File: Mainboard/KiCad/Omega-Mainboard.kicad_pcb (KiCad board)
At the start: 2 copper layers, 333.4 x 149.9 mm, 248 parts, among them J1 5V, J10 POWER, J11 KEYBOARD, J12 RAM_EXT, J13 ~RST~/~NMI, J14 CBUS, J2 Composite, J3 Audio, J4 S-VIDEO, J5 RGB, J6 Cassette, J7 JOYSTICK_A, J8 JOYSTICK_B, J9 PRINTER, Q1 PN2907A, Q2 PN2907A, U1 Z84C00, U10 D41464, U11 D41464, U12 ATF16V8B, U13 ATF16V8B, U14 ATF16V8B, U15 74HCT670, U16 74HCT670, U17 74HCT670, U18 74HCT670, U19 74F541, U2 82C55, U20 74F541, U21 74F541, U22 74HCT540, U23 74HCT273, U24 74HCT273, U25 74F245, U26 74F245, U27 74HCT175, U28 74HCT157, U29 74HCT157, U3 V9938/V9958, U30 74HCT153, U31 74HCT153, U32 74AHCT138, U33 74AHCT125, U34 74HCT74, U35 74HCT74, U36 74HCT74, U37 74AHCT32, U38 74AHCT32, U39 74AHCT32, U4 YM2149, U40 74HCT30, U41 74HCT30, U42 74LS07, U43 74HCT04, U44 74AHCT02, U45 74HCT00, U46 ADM691A, U47 CXA1645, U48 MCP6281, U49 LM311, U5 RP5C01, U6 SST39SF040, U7 AS6C4008, U8 D41464, U9 D41464, Y1 21.477270MHz, Y2 32768 Hz, Y3 4.433618MHz

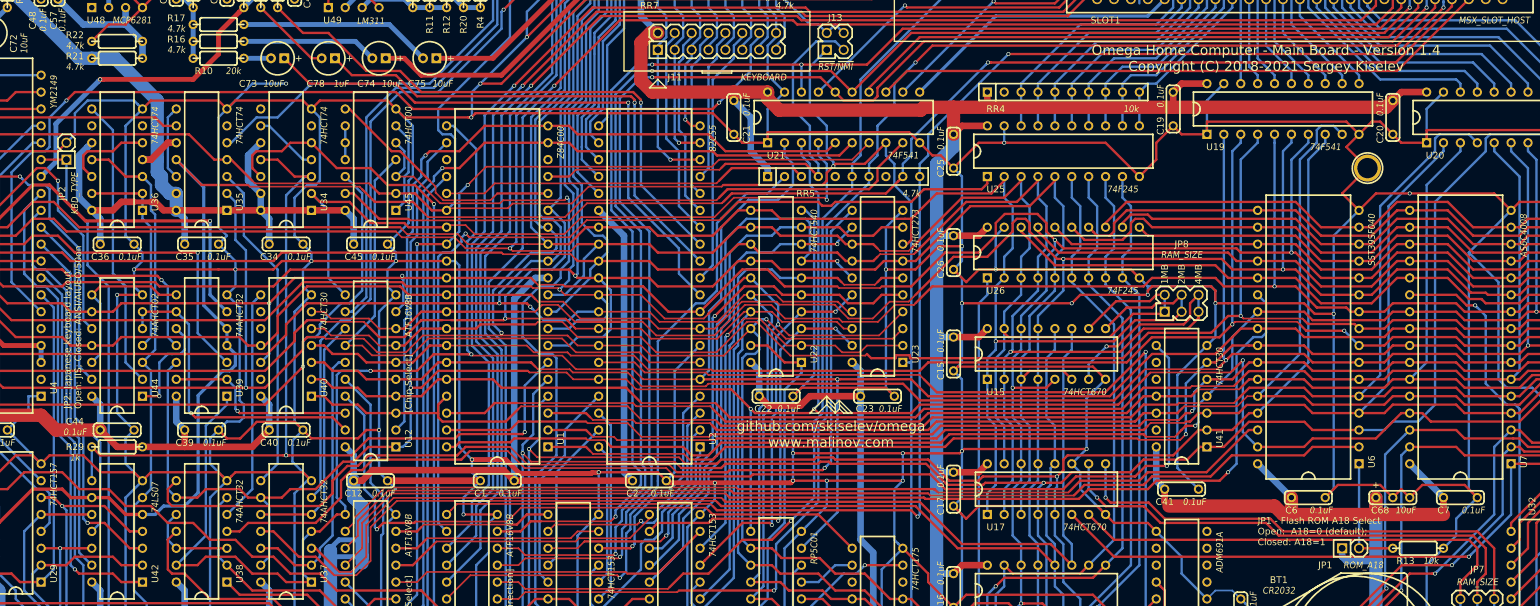
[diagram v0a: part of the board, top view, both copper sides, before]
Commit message: Fix issue #56, where joystick A trigger 2 was swapped with joystick B trigger 1
Signed-off-by: Sergey Kiselev <skiselev@gmail.com>
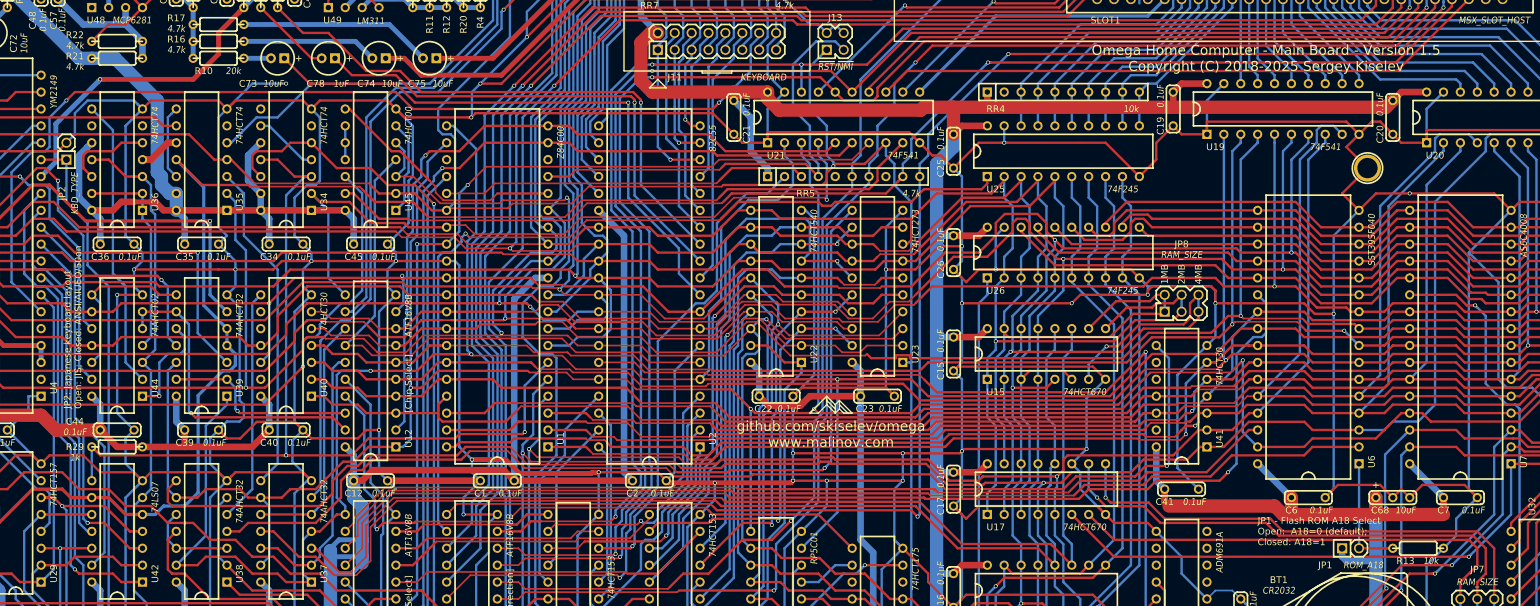
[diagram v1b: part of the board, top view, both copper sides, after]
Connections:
- U42 pad 11: /PSG/JB2 -> /PSG/JB1
- U42 pad 13: /PSG/JB1 -> /PSG/JB2
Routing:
- net /PSG/JB2: track 49.9 -> 55.5 mm
- net /PSG/JB1: track 58.3 -> 53.6 mm
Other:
- board text added: "Omega Home Computer - Main Board - Version 1.5 Copyright (C) 2018-2025 Sergey Kiselev"
- board text removed: "Omega Home Computer - Main Board - Version 1.4 Copyright (C) 2018-2021 Sergey Kiselev"

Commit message: Update gerber files for version 1.5
Signed-off-by: Sergey Kiselev <skiselev@gmail.com>
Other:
- rule pad_to_mask_clearance: 0.2 -> 0
